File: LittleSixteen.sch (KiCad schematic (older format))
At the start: 19 parts

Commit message: Rationalize capacitor footprints & BOM
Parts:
- H1, H10, H11, H12, H13, H14, H15, H16, H2, H3, H4, H5, H6, H7, H8, H9: MouserPN (none) -> ---
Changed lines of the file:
@@
 F 2 "MountingHole:MountingHole_3.7mm_Pad" H 10275 4605 50  0001 C CNN
 F 3 "~" H 10275 4605 50  0001 C CNN
+F 4 "---" H 10275 4605 50  0001 C CNN "MouserPN"
 	1    10275 4605
 	1    0    0    -1
@@
 F 2 "MountingHole:MountingHole_3.7mm_Pad" H 10275 4915 50  0001 C CNN
 F 3 "~" H 10275 4915 50  0001 C CNN
+F 4 "---" H 10275 4915 50  0001 C CNN "MouserPN"
 	1    10275 4915
 	1    0    0    -1
@@
 F 2 "" H 10275 5235 50  0001 C CNN
 F 3 "~" H 10275 5235 50  0001 C CNN
+F 4 "---" H 10275 5235 50  0001 C CNN "MouserPN"
 	1    10275 5235
 	1    0    0    -1
@@
 F 2 "MountingHole:MountingHole_3.7mm_Pad" H 10275 5560 50  0001 C CNN
 F 3 "~" H 10275 5560 50  0001 C CNN
+F 4 "---" H 10275 5560 50  0001 C CNN "MouserPN"
 	1    10275 5560
 	1    0    0    -1
@@
 F 2 "MountingHole:MountingHole_4.3mm_M4_Pad" H 10275 5885 50  0001 C CNN
 F 3 "~" H 10275 5885 50  0001 C CNN
+F 4 "---" H 10275 5885 50  0001 C CNN "MouserPN"
 	1    10275 5885
 	1    0    0    -1
@@
 F 2 "MountingHole:MountingHole_3.7mm_Pad" H 10785 4605 50  0001 C CNN
 F 3 "~" H 10785 4605 50  0001 C CNN
+F 4 "---" H 10785 4605 50  0001 C CNN "MouserPN"
 	1    10785 4605
 	1    0    0    -1
@@
 F 2 "MountingHole:MountingHole_3.7mm_Pad" H 10785 4915 50  0001 C CNN
 F 3 "~" H 10785 4915 50  0001 C CNN
+F 4 "---" H 10785 4915 50  0001 C CNN "MouserPN"
 	1    10785 4915
 	1    0    0    -1
@@
 F 2 "MountingHole:MountingHole_3.7mm_Pad" H 10785 5235 50  0001 C CNN
 F 3 "~" H 10785 5235 50  0001 C CNN
+F 4 "---" H 10785 5235 50  0001 C CNN "MouserPN"
 	1    10785 5235
 	1    0    0    -1
@@
 F 2 "" H 10785 5560 50  0001 C CNN
 F 3 "~" H 10785 5560 50  0001 C CNN
+F 4 "---" H 10785 5560 50  0001 C CNN "MouserPN"
 	1    10785 5560
 	1    0    0    -1
@@
 F 2 "MountingHole:MountingHole_4.3mm_M4_Pad" H 10785 5885 50  0001 C CNN
 F 3 "~" H 10785 5885 50  0001 C CNN
+F 4 "---" H 10785 5885 50  0001 C CNN "MouserPN"
 	1    10785 5885
 	1    0    0    -1
@@
 F 2 "MountingHole:MountingHole_2.7mm_Pad" H 9750 4605 50  0001 C CNN
 F 3 "~" H 9750 4605 50  0001 C CNN
+F 4 "---" H 9750 4605 50  0001 C CNN "MouserPN"
 	1    9750 4605
 	1    0    0    -1
@@
 F 2 "MountingHole:MountingHole_2.7mm_Pad" H 9750 4915 50  0001 C CNN
 F 3 "~" H 9750 4915 50  0001 C CNN
+F 4 "---" H 9750 4915 50  0001 C CNN "MouserPN"
 	1    9750 4915
 	1    0    0    -1
@@
 F 2 "MountingHole:MountingHole_2.7mm_Pad" H 9750 5235 50  0001 C CNN
 F 3 "~" H 9750 5235 50  0001 C CNN
+F 4 "---" H 9750 5235 50  0001 C CNN "MouserPN"
 	1    9750 5235
 	1    0    0    -1
@@
 F 2 "MountingHole:MountingHole_2.7mm_Pad" H 9750 5560 50  0001 C CNN
 F 3 "~" H 9750 5560 50  0001 C CNN
+F 4 "---" H 9750 5560 50  0001 C CNN "MouserPN"
 	1    9750 5560
 	1    0    0    -1
@@
 F 2 "MountingHole:MountingHole_3.7mm_Pad" H 9205 4605 50  0001 C CNN
 F 3 "~" H 9205 4605 50  0001 C CNN
+F 4 "---" H 9205 4605 50  0001 C CNN "MouserPN"
 	1    9205 4605
 	1    0    0    -1
@@
 F 2 "MountingHole:MountingHole_3.7mm_Pad" H 9205 4915 50  0001 C CNN
 F 3 "~" H 9205 4915 50  0001 C CNN
+F 4 "---" H 9205 4915 50  0001 C CNN "MouserPN"
 	1    9205 4915
 	1    0    0    -1

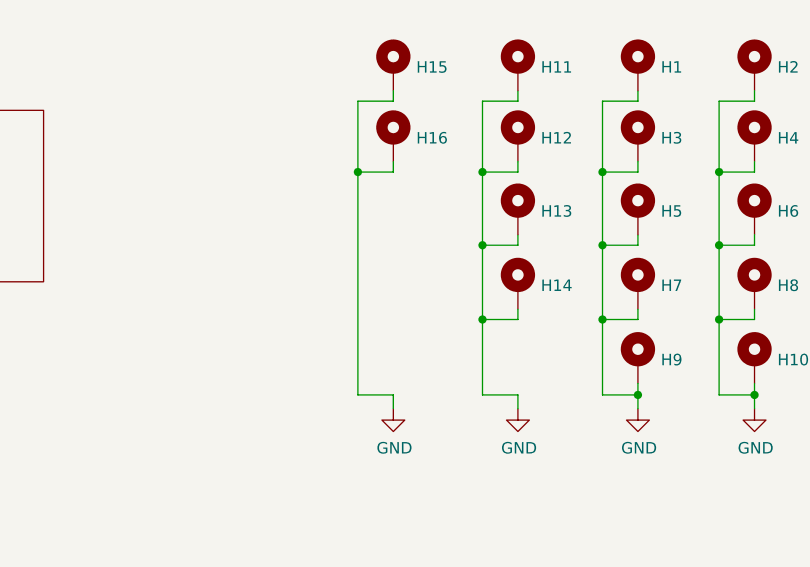
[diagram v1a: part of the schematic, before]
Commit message: Fix screw holes for C16 case
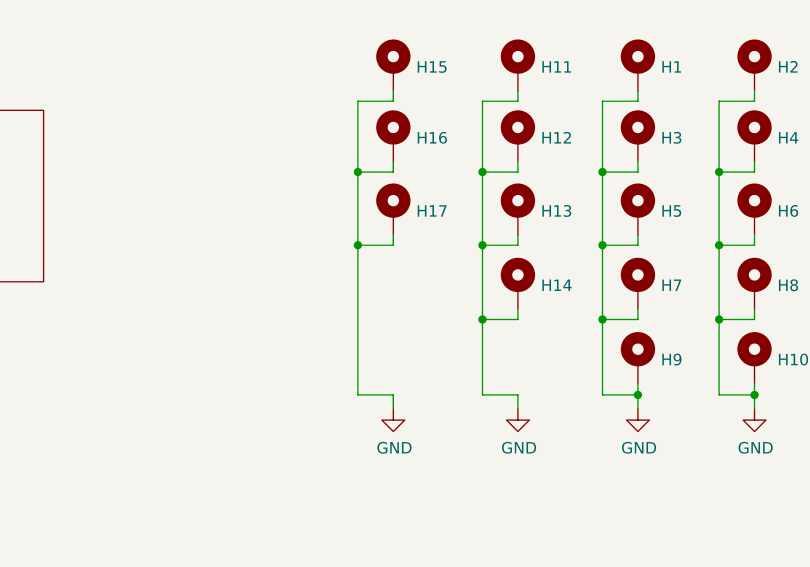
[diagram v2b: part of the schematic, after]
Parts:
- added H17: MountingHole_Pad, MountingHole:MountingHole_3.7mm_Pad, symbol Mechanical:MountingHole_Pad
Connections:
- net GND: now also H17.1
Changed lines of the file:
@@
 	9050 4750 9050 5060
 Wire Wire Line
-	9050 5060 9050 6035
+	9050 5060 9050 5380
+$Comp
+L Mechanical:MountingHole_Pad H17
+U 1 1 67204BC1
+P 9205 5235
+F 0 "H17" H 9305 5238 50  0000 L CNN
+F 1 "MountingHole_Pad" H 9305 5193 50  0001 L CNN
+F 2 "MountingHole:MountingHole_3.7mm_Pad" H 9205 5235 50  0001 C CNN
+F 3 "~" H 9205 5235 50  0001 C CNN
+F 4 "---" H 9205 5235 50  0001 C CNN "MouserPN"
+	1    9205 5235
+	1    0    0    -1
+$EndComp
+Wire Wire Line
+	9205 5335 9205 5380
+Wire Wire Line
+	9205 5380 9050 5380
+Connection ~ 9050 5380
+Wire Wire Line
+	9050 5380 9050 6035
 $EndSCHEMATC

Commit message: Minor fixes + P/N updates
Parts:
- V0, V1, V2: MouserPN (none) -> ---
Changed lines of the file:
@@
 F 2 "LittleSixteen:Logo" H 6030 7170 50  0001 C CNN
 F 3 "" H 6030 7170 50  0001 C CNN
+F 4 "---" H 6030 7170 50  0001 C CNN "MouserPN"
 	1    6030 7170
 	1    0    0    -1
@@
 F 2 "LittleSixteen:cc_by_nc_sa" H 6030 7590 50  0001 C CNN
 F 3 "" H 6030 7590 50  0001 C CNN
+F 4 "---" H 6030 7590 50  0001 C CNN "MouserPN"
 	1    6030 7590
 	1    0    0    -1
@@
 F 2 "LittleSixteen:pcbway" H 6030 7380 50  0001 C CNN
 F 3 "" H 6030 7380 50  0001 C CNN
+F 4 "---" H 6030 7380 50  0001 C CNN "MouserPN"
 	1    6030 7380
 	1    0    0    -1
